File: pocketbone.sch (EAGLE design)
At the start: 60 parts, among them J1 USD_CONNECTOR, U1 24LC_32AT-I/OT, U2 OSD3358, U3 SN74LVC1G07_DCK_5, Y1 CM200C-32.768KAZF-UT, Y2 445C33D24M00000

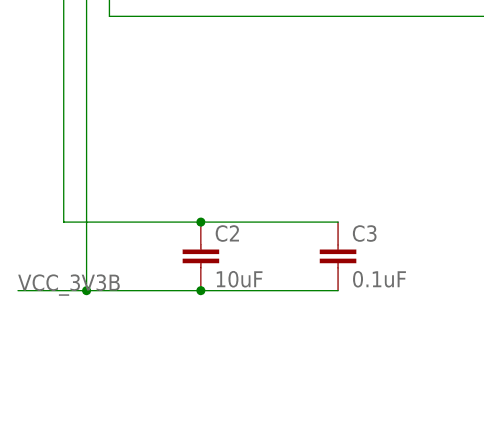
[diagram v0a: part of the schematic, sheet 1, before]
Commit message: Connect microSD to 3.3V
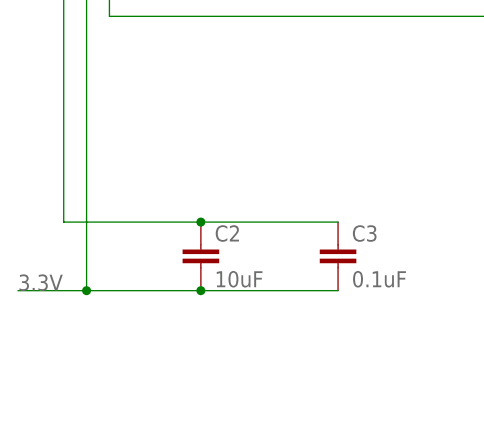
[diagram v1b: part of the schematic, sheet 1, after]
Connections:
- removed net VCC_3V3B: C2.2, C3.2, J1.VCC
- net 3.3V: now also C2.2, C3.2, J1.VCC
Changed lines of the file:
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@@
 <label x="281.94" y="248.92" size="1.778" layer="95"/>
+</segment>
+<segment>
+<wire x1="10.16" y1="20.32" x2="17.78" y2="20.32" width="0.1524" layer="91"/>
+<wire x1="17.78" y1="20.32" x2="30.48" y2="20.32" width="0.1524" layer="91"/>
+<wire x1="30.48" y1="20.32" x2="45.72" y2="20.32" width="0.1524" layer="91"/>
+<label x="10.16" y="20.32" size="1.778" layer="95"/>
+<pinref part="C3" gate="G$1" pin="2"/>
+<pinref part="C2" gate="G$1" pin="2"/>
+<junction x="30.48" y="20.32"/>
+<pinref part="J1" gate="1" pin="VCC"/>
+<wire x1="27.94" y1="83.82" x2="17.78" y2="83.82" width="0.1524" layer="91"/>
+<wire x1="17.78" y1="83.82" x2="17.78" y2="20.32" width="0.1524" layer="91"/>
+<junction x="17.78" y="20.32"/>
 </segment>
 </net>
@@
 </segment>
 </net>
-<net name="VCC_3V3B" class="0">
-<segment>
-<wire x1="10.16" y1="20.32" x2="17.78" y2="20.32" width="0.1524" layer="91"/>
-<wire x1="17.78" y1="20.32" x2="30.48" y2="20.32" width="0.1524" layer="91"/>
-<wire x1="30.48" y1="20.32" x2="45.72" y2="20.32" width="0.1524" layer="91"/>
-<label x="10.16" y="20.32" size="1.778" layer="95"/>
-<pinref part="C3" gate="G$1" pin="2"/>
-<pinref part="C2" gate="G$1" pin="2"/>
-<junction x="30.48" y="20.32"/>
-<pinref part="J1" gate="1" pin="VCC"/>
-<wire x1="27.94" y1="83.82" x2="17.78" y2="83.82" width="0.1524" layer="91"/>
-<wire x1="17.78" y1="83.82" x2="17.78" y2="20.32" width="0.1524" layer="91"/>
-<junction x="17.78" y="20.32"/>
-</segment>
-</net>
